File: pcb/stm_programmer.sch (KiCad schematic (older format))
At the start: 37 parts

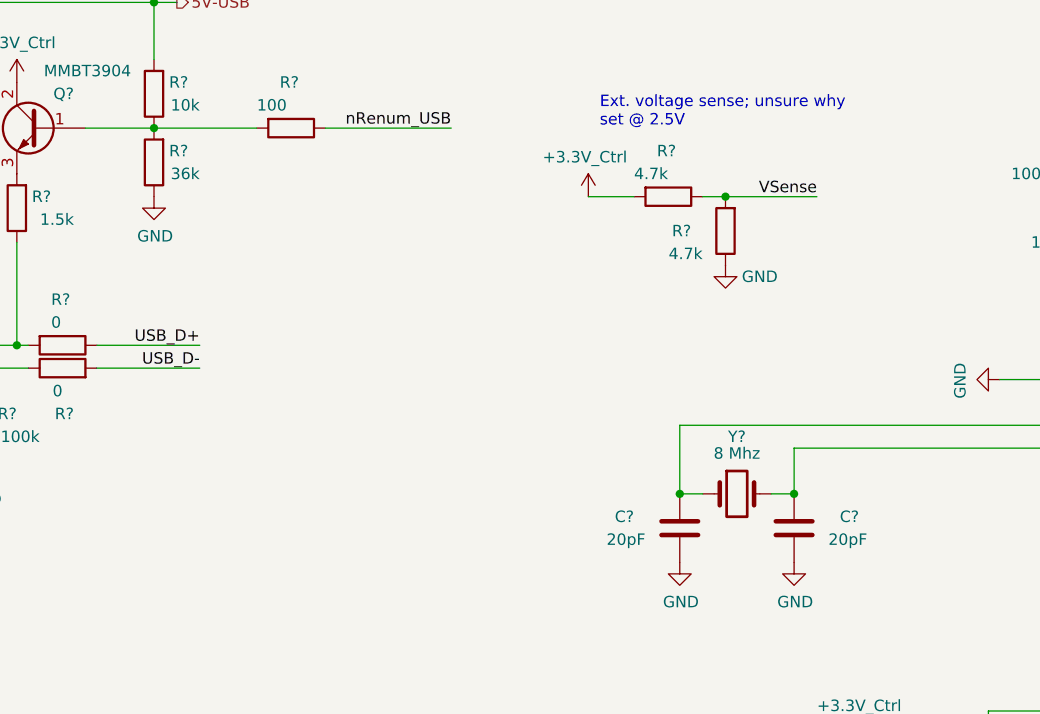
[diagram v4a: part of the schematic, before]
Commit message: BOM
More BOM consolidation with bulk capacitors + changed tantalum stepper caps to aluminum, added bulk cap to PSol driver
Made stepper's 3.3V power naming consistent with others (3.3V->3V3)
Slightly increased current limit on PSOL/heater driver
Changed 3906 transistors to 2907 to better support +5V_Batt current
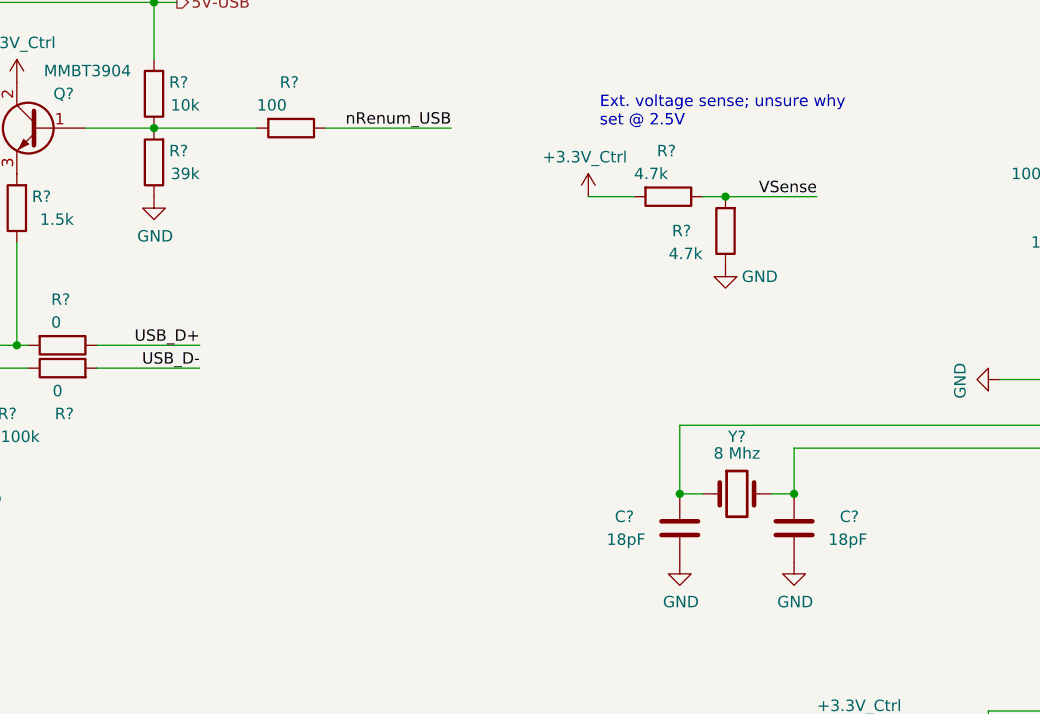
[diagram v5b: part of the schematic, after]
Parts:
- C? (x2): value 20pF -> 18pF; Dielectric (none) -> NP0
- D? (x2): footprint (none) -> RespiraWorks_Std:LED_0805_2012Metric
- J? (x2): footprint (none) -> RespiraWorks_Std:PinHeader_1x06_P2.54mm_Vertical
- R? (x2): footprint RespiraWorks_std:R_0603_1608Metric -> RespiraWorks_Std:R_0603_1608Metric
- R?: value 36k -> 39k
- Y?: Manufacturer (none) -> Abracon; Manufacturer PN (none) -> ABLS-8.000MHZ-B4-T
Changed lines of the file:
@@
 F 0 "R?" V 1750 2450 50  0000 L CNN
 F 1 "0" V 1850 2450 50  0000 L CNN
-F 2 "RespiraWorks_std:R_0603_1608Metric" V 1880 2500 50  0001 C CNN
+F 2 "RespiraWorks_Std:R_0603_1608Metric" V 1880 2500 50  0001 C CNN
 F 3 "~" H 1950 2500 50  0001 C CNN
 	1    1950 2500
@@
 F 0 "R?" V 1750 2550 50  0000 L CNN
 F 1 "0" V 1850 2600 50  0000 L CNN
-F 2 "RespiraWorks_std:R_0603_1608Metric" V 1880 2600 50  0001 C CNN
+F 2 "RespiraWorks_Std:R_0603_1608Metric" V 1880 2600 50  0001 C CNN
 F 3 "~" H 1950 2600 50  0001 C CNN
 	1    1950 2600
@@
 AR Path="/5FCD4D85/5FF3C26A" Ref="R?"  Part="1"
 F 0 "R?" H 2200 1650 50  0000 L CNN
-F 1 "36k" H 2150 1750 50  0000 L CNN
+F 1 "39k" H 2150 1750 50  0000 L CNN
 F 2 "RespiraWorks_Std:R_0603_1608Metric" V 2280 1700 50  0001 C CNN
 F 3 "~" H 2350 1700 50  0001 C CNN
@@
 F 0 "J?" H 1468 5767 50  0000 C CNN
 F 1 "Backup debug in for cycle controller" H 1750 5700 50  0000 C CNN
-F 2 "" H 1550 5350 50  0001 C CNN
+F 2 "RespiraWorks_Std:PinHeader_1x06_P2.54mm_Vertical" H 1550 5350 50  0001 C CNN
 F 3 "~" H 1550 5350 50  0001 C CNN
 	1    1550 5350
@@
 AR Path="/5FCD4D85/5FF56FF1" Ref="C?"  Part="1"
 F 0 "C?" H 4850 3250 50  0000 L CNN
-F 1 "20pF" H 4800 3350 50  0000 L CNN
+F 1 "18pF" H 4800 3350 50  0000 L CNN
 F 2 "RespiraWorks_Std:C_0603_1608Metric" H 4688 3150 50  0001 C CNN
 F 3 "~" H 4650 3300 50  0001 C CNN
+F 4 "NP0" H 4650 3300 50  0001 C CNN "Dielectric"
 	1    4650 3300
 	-1   0    0    1
@@
 AR Path="/5FCD4D85/5FF5ADBF" Ref="C?"  Part="1"
 F 0 "C?" H 5350 3250 50  0000 L CNN
-F 1 "20pF" H 5300 3350 50  0000 L CNN
+F 1 "18pF" H 5300 3350 50  0000 L CNN
 F 2 "RespiraWorks_Std:C_0603_1608Metric" H 5188 3150 50  0001 C CNN
 F 3 "~" H 5150 3300 50  0001 C CNN
+F 4 "NP0" H 5150 3300 50  0001 C CNN "Dielectric"
 	1    5150 3300
 	1    0    0    1
@@
 F 2 "RespiraWorks_Std:Crystal_SMD_HC49-SD" H 4900 3150 50  0001 C CNN
 F 3 "~" H 4900 3150 50  0001 C CNN
+F 4 "Abracon" H 4900 3150 50  0001 C CNN "Manufacturer"
+F 5 "ABLS-8.000MHZ-B4-T" H 4900 3150 50  0001 C CNN "Manufacturer PN"
 	1    4900 3150
 	1    0    0    -1
@@
 F 0 "J?" H 1468 7167 50  0000 C CNN
 F 1 "Debug in for ST-LINK" H 1468 7076 50  0000 C CNN
-F 2 "" H 1550 6750 50  0001 C CNN
+F 2 "RespiraWorks_Std:PinHeader_1x06_P2.54mm_Vertical" H 1550 6750 50  0001 C CNN
 F 3 "~" H 1550 6750 50  0001 C CNN
 	1    1550 6750
@@
 F 0 "D?" V 5489 5132 50  0000 R CNN
 F 1 "Red" V 5398 5132 50  0000 R CNN
-F 2 "" H 5450 5250 50  0001 C CNN
+F 2 "RespiraWorks_Std:LED_0805_2012Metric" H 5450 5250 50  0001 C CNN
 F 3 "~" H 5450 5250 50  0001 C CNN
 	1    5450 5250
@@
 F 0 "D?" V 5489 4582 50  0000 R CNN
 F 1 "Green" V 5398 4582 50  0000 R CNN
-F 2 "" H 5450 4700 50  0001 C CNN
+F 2 "RespiraWorks_Std:LED_0805_2012Metric" H 5450 4700 50  0001 C CNN
 F 3 "~" H 5450 4700 50  0001 C CNN
 	1    5450 4700

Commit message: BOM, fixes
Finished assigning parts, footprints except generic resistors
Added series resistors for logic signals received by UI computer to protect against UI computer power-down
Added tolerance notes on main schem
Replaced PSol fuse with PTC
Enlarged PSol driver bypass resistors to 0 ohm
Changed PSol unpopulated current-limiting resistor to divider
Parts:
- C? (x5): Dielectric (none) -> X7R; Manufacturer (none) -> Kemet; Manufacturer PN (none) -> C0603C104K5RACTU; Voltage (none) -> 50V
- C? (x2): Manufacturer (none) -> Kemet; Manufacturer PN (none) -> C0603C180J5GACTU; Voltage (none) -> 50V
- D?: Manufacturer (none) -> Lite-On; Manufacturer PN (none) -> LTST-C170KRKT
- D?: Manufacturer (none) -> Lite-On; Manufacturer PN (none) -> LTST-C171KGKT
- J?: footprint (none) -> RespiraWorks_Std:USB_Mini-B_Wuerth_65100516121_Horizontal; Manufacturer (none) -> Wuerth Elektronik; Manufacturer PN (none) -> 65100516121
- J? (x2): Manufacturer (none) -> Harwin; Manufacturer PN (none) -> M20-9980345
- Q?: Manufacturer (none) -> Diodes Inc.; Manufacturer PN (none) -> MMBT3904-7-F
- U?: Manufacturer (none) -> STMicroelectronics; Manufacturer PN (none) -> STM32F103CBT6
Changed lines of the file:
@@
 $Descr A4 11693 8268
 encoding utf-8
-Sheet 37 38
+Sheet 38 38
 Title "STM Programmer for Cycle Controller"
 Date ""
@@
 F 2 "RespiraWorks_Std:LQFP-48_7x7mm_P0.5mm" H 7150 2000 50  0001 R CNN
 F 3 "" H 7700 3350 50  0001 C CNN
+F 4 "STMicroelectronics" H 7750 3700 50  0001 C CNN "Manufacturer"
+F 5 "STM32F103CBT6" H 7750 3700 50  0001 C CNN "Manufacturer PN"
 	1    7750 3700
 	1    0    0    -1
@@
 F 2 "RespiraWorks_Std:C_0603_1608Metric" H 8288 1450 50  0001 C CNN
 F 3 "~" H 8250 1600 50  0001 C CNN
+F 4 "X7R" H 8250 1600 50  0001 C CNN "Dielectric"
+F 5 "Kemet" H 8250 1600 50  0001 C CNN "Manufacturer"
+F 6 "C0603C104K5RACTU" H 8250 1600 50  0001 C CNN "Manufacturer PN"
+F 7 "50V" H 8250 1600 50  0001 C CNN "Voltage"
 	1    8250 1600
 	-1   0    0    1
@@
 F 2 "RespiraWorks_Std:C_0603_1608Metric" H 8688 1450 50  0001 C CNN
 F 3 "~" H 8650 1600 50  0001 C CNN
+F 4 "X7R" H 8650 1600 50  0001 C CNN "Dielectric"
+F 5 "Kemet" H 8650 1600 50  0001 C CNN "Manufacturer"
+F 6 "C0603C104K5RACTU" H 8650 1600 50  0001 C CNN "Manufacturer PN"
+F 7 "50V" H 8650 1600 50  0001 C CNN "Voltage"
 	1    8650 1600
 	-1   0    0    1
@@
 F 2 "RespiraWorks_Std:C_0603_1608Metric" H 9088 1450 50  0001 C CNN
 F 3 "~" H 9050 1600 50  0001 C CNN
+F 4 "X7R" H 9050 1600 50  0001 C CNN "Dielectric"
+F 5 "Kemet" H 9050 1600 50  0001 C CNN "Manufacturer"
+F 6 "C0603C104K5RACTU" H 9050 1600 50  0001 C CNN "Manufacturer PN"
+F 7 "50V" H 9050 1600 50  0001 C CNN "Voltage"
 	1    9050 1600
 	-1   0    0    1
@@
 F 2 "RespiraWorks_Std:C_0603_1608Metric" H 9488 1450 50  0001 C CNN
 F 3 "~" H 9450 1600 50  0001 C CNN
+F 4 "X7R" H 9450 1600 50  0001 C CNN "Dielectric"
+F 5 "Kemet" H 9450 1600 50  0001 C CNN "Manufacturer"
+F 6 "C0603C104K5RACTU" H 9450 1600 50  0001 C CNN "Manufacturer PN"
+F 7 "50V" H 9450 1600 50  0001 C CNN "Voltage"
 	1    9450 1600
 	-1   0    0    1
@@
 F 2 "RespiraWorks_Std:C_0603_1608Metric" H 6588 1850 50  0001 C CNN
 F 3 "~" H 6550 2000 50  0001 C CNN
+F 4 "X7R" H 6550 2000 50  0001 C CNN "Dielectric"
+F 5 "Kemet" H 6550 2000 50  0001 C CNN "Manufacturer"
+F 6 "C0603C104K5RACTU" H 6550 2000 50  0001 C CNN "Manufacturer PN"
+F 7 "50V" H 6550 2000 50  0001 C CNN "Voltage"
 	1    6550 2000
 	-1   0    0    1
@@
 F 0 "J?" H 1050 2950 50  0000 C CNN
 F 1 "USB B micro" H 1150 2850 50  0000 C CNN
-F 2 "" H 1300 2450 50  0001 C CNN
+F 2 "RespiraWorks_Std:USB_Mini-B_Wuerth_65100516121_Horizontal" H 1300 2450 50  0001 C CNN
 F 3 "~" H 1300 2450 50  0001 C CNN
+F 4 "Wuerth Elektronik" H 1150 2500 50  0001 C CNN "Manufacturer"
+F 5 "65100516121" H 1150 2500 50  0001 C CNN "Manufacturer PN"
 	1    1150 2500
 	1    0    0    -1
@@
 F 2 "RespiraWorks_Std:SOT-23" H 2050 1650 50  0001 C CNN
 F 3 "~" H 1850 1550 50  0001 C CNN
+F 4 "Diodes Inc." H 1850 1550 50  0001 C CNN "Manufacturer"
+F 5 "MMBT3904-7-F" H 1850 1550 50  0001 C CNN "Manufacturer PN"
 	1    1850 1550
 	-1   0    0    -1
@@
 F 2 "RespiraWorks_Std:PinHeader_1x06_P2.54mm_Vertical" H 1550 5350 50  0001 C CNN
 F 3 "~" H 1550 5350 50  0001 C CNN
+F 4 "Harwin" H 1550 5350 50  0001 C CNN "Manufacturer"
+F 5 "M20-9980345" H 1550 5350 50  0001 C CNN "Manufacturer PN"
 	1    1550 5350
 	-1   0    0    -1
@@
 F 3 "~" H 4650 3300 50  0001 C CNN
 F 4 "NP0" H 4650 3300 50  0001 C CNN "Dielectric"
+F 5 "Kemet" H 4650 3300 50  0001 C CNN "Manufacturer"
+F 6 "C0603C180J5GACTU" H 4650 3300 50  0001 C CNN "Manufacturer PN"
+F 7 "50V" H 4650 3300 50  0001 C CNN "Voltage"
 	1    4650 3300
 	-1   0    0    1
@@
 F 3 "~" H 5150 3300 50  0001 C CNN
 F 4 "NP0" H 5150 3300 50  0001 C CNN "Dielectric"
+F 5 "Kemet" H 5150 3300 50  0001 C CNN "Manufacturer"
+F 6 "C0603C180J5GACTU" H 5150 3300 50  0001 C CNN "Manufacturer PN"
+F 7 "50V" H 5150 3300 50  0001 C CNN "Voltage"
 	1    5150 3300
 	1    0    0    1
@@
 F 2 "RespiraWorks_Std:PinHeader_1x06_P2.54mm_Vertical" H 1550 6750 50  0001 C CNN
 F 3 "~" H 1550 6750 50  0001 C CNN
+F 4 "Harwin" H 1550 6750 50  0001 C CNN "Manufacturer"
+F 5 "M20-9980345" H 1550 6750 50  0001 C CNN "Manufacturer PN"
 	1    1550 6750
 	-1   0    0    -1
@@
 F 2 "RespiraWorks_Std:LED_0805_2012Metric" H 5450 5250 50  0001 C CNN
 F 3 "~" H 5450 5250 50  0001 C CNN
+F 4 "Lite-On" H 5450 5250 50  0001 C CNN "Manufacturer"
+F 5 "LTST-C170KRKT" H 5450 5250 50  0001 C CNN "Manufacturer PN"
 	1    5450 5250
 	0    -1   -1   0
@@
 F 2 "RespiraWorks_Std:LED_0805_2012Metric" H 5450 4700 50  0001 C CNN
 F 3 "~" H 5450 4700 50  0001 C CNN
+F 4 "Lite-On" H 5450 4700 50  0001 C CNN "Manufacturer"
+F 5 "LTST-C171KGKT" H 5450 4700 50  0001 C CNN "Manufacturer PN"
 	1    5450 4700
 	0    -1   -1   0

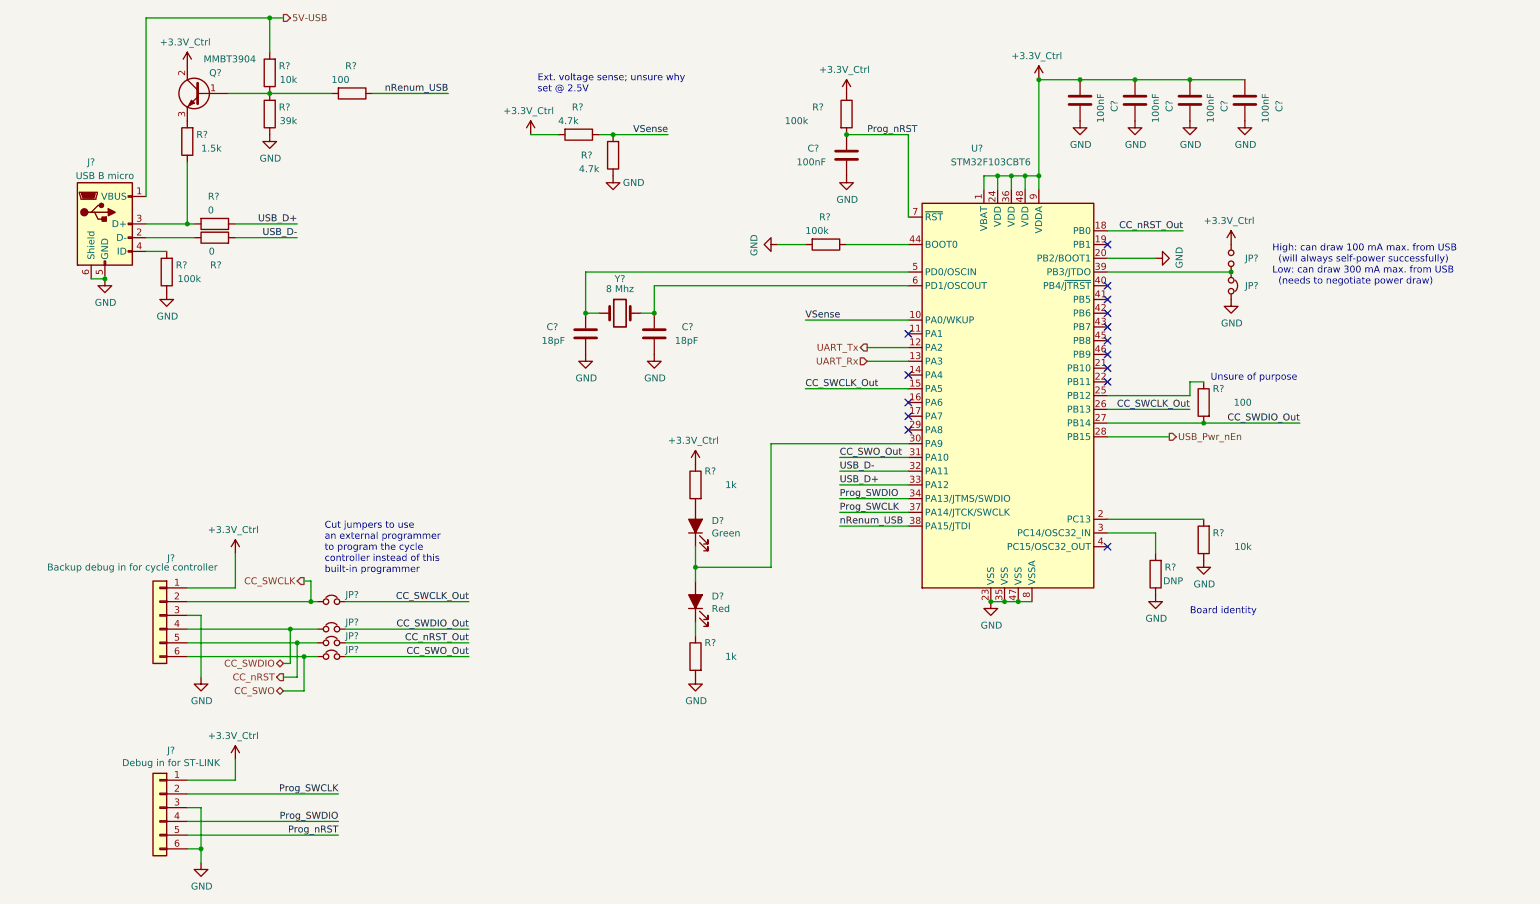
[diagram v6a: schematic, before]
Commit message: Stephanie fixes, net names
Removed duplicate global I2C pull-ups
Added missing BMP280 pin 7
Correcting pin names etc. on LM4120 voltage reference
Finished standardizing net names
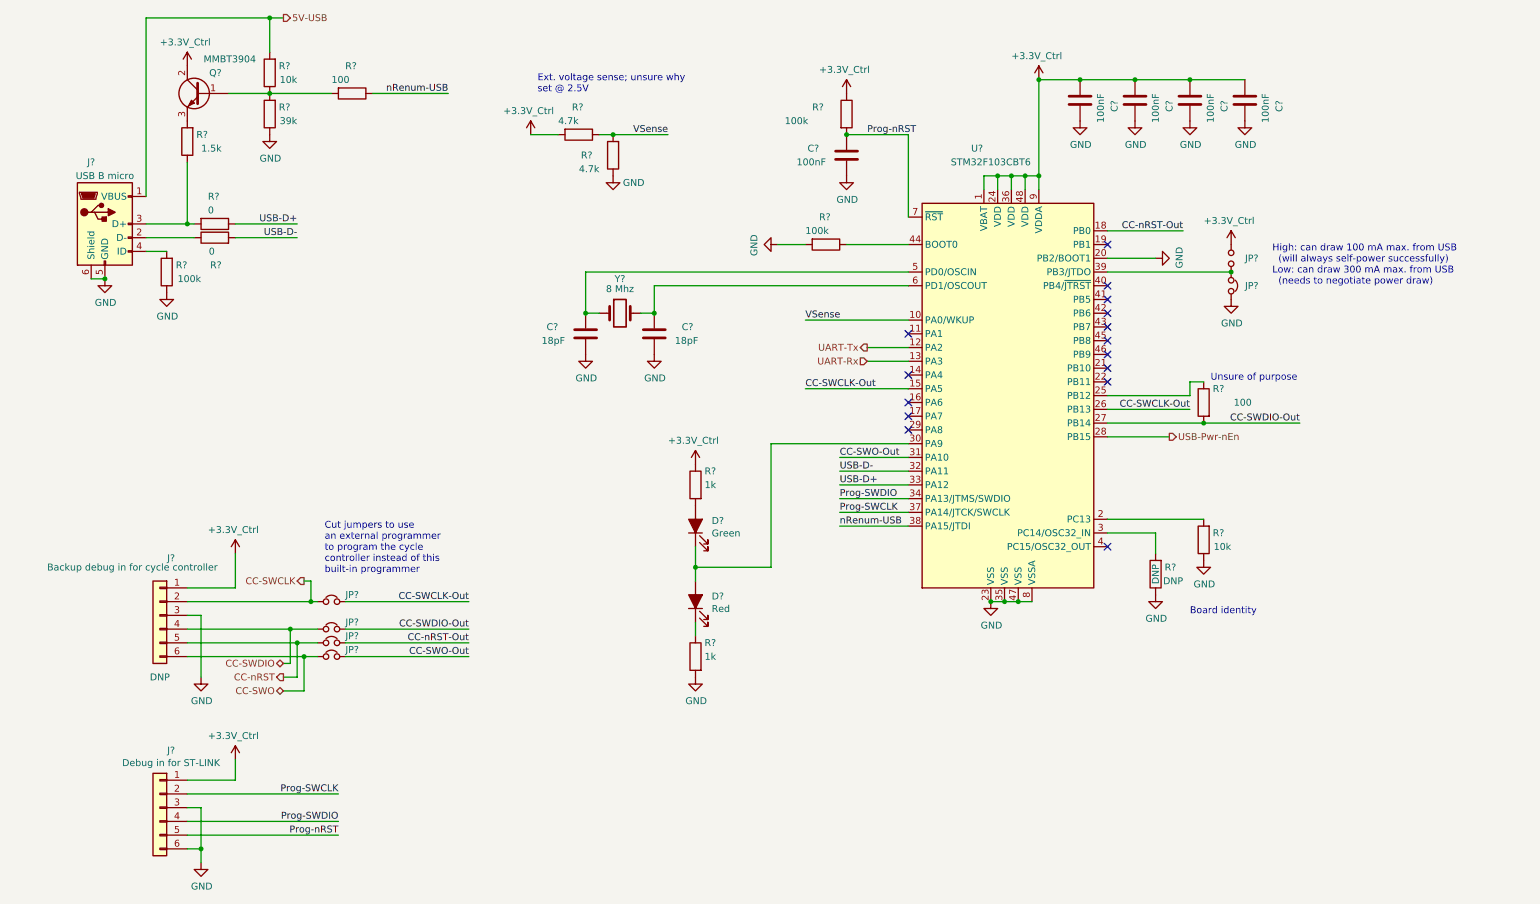
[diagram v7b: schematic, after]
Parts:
- J?: DNP (none) -> DNP
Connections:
- net CC_SWCLK renamed CC-SWCLK
- net CC_SWCLK_Out renamed CC-SWCLK-Out
- net CC_SWDIO renamed CC-SWDIO
- net CC_SWDIO_Out renamed CC-SWDIO-Out
- net CC_SWO renamed CC-SWO
- net CC_SWO_Out renamed CC-SWO-Out
- net CC_nRST renamed CC-nRST
- net CC_nRST_Out renamed CC-nRST-Out
- net Prog_SWCLK renamed Prog-SWCLK
- net Prog_SWDIO renamed Prog-SWDIO
- net Prog_nRST renamed Prog-nRST
- net UART_Rx renamed UART-Rx
- net UART_Tx renamed UART-Tx
- net USB_D+ renamed USB-D+
- net USB_D- renamed USB-D-
- net USB_Pwr_nEn renamed USB-Pwr-nEn
- net nRenum_USB renamed nRenum-USB
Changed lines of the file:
@@
 	1800 2500 1750 2500
 Text Label 2550 2600 2    50   ~ 0
-USB_D-
+USB-D-
 Text Label 2550 2500 2    50   ~ 0
-USB_D+
+USB-D+
 Wire Wire Line
 	2100 2500 2550 2500
@@
 	7000 4300 6500 4300
 Text Label 6500 4400 0    50   ~ 0
-USB_D+
+USB-D+
 Text Label 6500 4300 0    50   ~ 0
-USB_D-
+USB-D-
 $Comp
 L Device:R R?
@@
 	2800 1550 2350 1550
 Text Label 3650 1550 2    50   ~ 0
-nRenum_USB
+nRenum-USB
 Wire Wire Line
 	3100 1550 3650 1550
@@
 	7000 4700 6500 4700
 Text Label 6500 4700 0    50   ~ 0
-nRenum_USB
+nRenum-USB
 $Comp
 L Connector_Generic:Conn_01x06 J?
@@
 F 4 "Harwin" H 1550 5350 50  0001 C CNN "Manufacturer"
 F 5 "M20-9980345" H 1550 5350 50  0001 C CNN "Manufacturer PN"
+F 6 "DNP" H 1550 4900 50  0000 C CNN "DNP"
 	1    1550 5350
 	-1   0    0    -1
@@
 	7000 3700 6250 3700
 Text Label 6250 3700 0    50   ~ 0
-CC_SWCLK_Out
+CC-SWCLK-Out
 Text Label 3800 5250 2    50   ~ 0
-CC_SWCLK_Out
+CC-SWCLK-Out
 $Comp
 L Device:Jumper_NC_Small JP?
@@
 	2900 5650 3800 5650
 Text Label 3800 5450 2    50   ~ 0
-CC_SWDIO_Out
+CC-SWDIO-Out
 Text Label 3800 5550 2    50   ~ 0
-CC_nRST_Out
+CC-nRST-Out
 Text Label 3800 5650 2    50   ~ 0
-CC_SWO_Out
+CC-SWO-Out
 Wire Wire Line
 	9050 3750 9050 3650
@@
 	8450 3950 9150 3950
 Text Label 9850 3950 2    50   ~ 0
-CC_SWDIO_Out
+CC-SWDIO-Out
 Text Label 9000 2550 2    50   ~ 0
-CC_nRST_Out
+CC-nRST-Out
 Wire Wire Line
 	7000 4200 6500 4200
 Text Label 6500 4200 0    50   ~ 0
-CC_SWO_Out
+CC-SWO-Out
 Wire Wire Line
 	7000 4500 6500 4500
 Text Label 6500 4500 0    50   ~ 0
-Prog_SWDIO
+Prog-SWDIO
 Wire Wire Line
 	7000 4600 6500 4600
 Text Label 6500 4600 0    50   ~ 0
-Prog_SWCLK
+Prog-SWCLK
 Text Label 6700 1850 0    50   ~ 0
-Prog_nRST
+Prog-nRST
 $Comp
 L Connector_Generic:Conn_01x06 J?
@@
 	1750 6850 2850 6850
 Text Label 2850 6650 2    50   ~ 0
-Prog_SWCLK
+Prog-SWCLK
 Text Label 2850 6850 2    50   ~ 0
-Prog_SWDIO
+Prog-SWDIO
 Text Label 2850 6950 2    50   ~ 0
-Prog_nRST
+Prog-nRST
 Wire Wire Line
 	1750 7050 1850 7050
@@
 AR Path="/5FCD4D85/5FFEED71" Ref="R?"  Part="1"
 F 0 "R?" H 5300 4500 50  0000 L CNN
-F 1 "1k" H 5150 4400 50  0000 L CNN
+F 1 "1k" H 5300 4400 50  0000 L CNN
 F 2 "RespiraWorks_Std:R_0603_1608Metric" V 5380 4400 50  0001 C CNN
 F 3 "~" H 5450 4400 50  0001 C CNN
@@
 AR Path="/5FCD4D85/5FFEF31C" Ref="R?"  Part="1"
 F 0 "R?" H 5300 5750 50  0000 L CNN
-F 1 "1k" H 5150 5650 50  0000 L CNN
+F 1 "1k" H 5300 5650 50  0000 L CNN
 F 2 "RespiraWorks_Std:R_0603_1608Metric" V 5380 5650 50  0001 C CNN
 F 3 "~" H 5450 5650 50  0001 C CNN
@@
 $EndComp
 Text HLabel 2600 5100 0    50   Output ~ 0
-CC_SWCLK
+CC-SWCLK
 Text HLabel 2450 5700 0    50   BiDi ~ 0
-CC_SWDIO
+CC-SWDIO
 Text HLabel 2450 5800 0    50   Output ~ 0
-CC_nRST
+CC-nRST
 Text HLabel 2450 5900 0    50   BiDi ~ 0
-CC_SWO
+CC-SWO
 Wire Wire Line
 	2450 5700 2500 5700
@@
 AR Path="/5FCD4D85/6007ED35" Ref="R?"  Part="1"
 F 0 "R?" H 9000 4750 50  0000 L CNN
-F 1 "10k" H 8800 4850 50  0000 L CNN
+F 1 "10k" H 8950 4850 50  0000 L CNN
 F 2 "RespiraWorks_Std:R_0603_1608Metric" V 9080 4800 50  0001 C CNN
 F 3 "~" H 9150 4800 50  0001 C CNN
@@
 F 2 "RespiraWorks_Std:R_0603_1608Metric" V 8730 5050 50  0001 C CNN
 F 3 "~" H 8800 5050 50  0001 C CNN
-F 4 "DNP" H 8800 5050 50  0001 C CNN "DNP"
+F 4 "DNP" V 8800 5050 50  0000 C CNN "DNP"
 	1    8800 5050
 	-1   0    0    1
@@
 	8450 4050 8900 4050
 Text HLabel 8900 4050 2    50   Output ~ 0
-USB_Pwr_nEn
+USB-Pwr-nEn
 Text Label 5250 1850 2    50   ~ 0
 VSense
@@
 	7000 3500 6700 3500
 Text HLabel 6700 3400 0    50   Output ~ 0
-UART_Tx
+UART-Tx
 Text HLabel 6700 3500 0    50   Input ~ 0
-UART_Rx
+UART-Rx
 NoConn ~ 8450 2650
 NoConn ~ 8450 2950
@@
 Cut jumpers to use\nan external programmer\nto program the cycle\ncontroller instead of this\nbuilt-in programmer
 Text Label 9050 3850 2    50   ~ 0
-CC_SWCLK_Out
+CC-SWCLK-Out
 Wire Wire Line
 	8450 3850 9050 3850
